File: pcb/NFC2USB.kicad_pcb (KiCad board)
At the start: 4 copper layers, 39 x 40 mm, 44 parts, among them J1 USB_C_USB2.0, SW1 BOOTSEL, SW2 MODE, U1 NFCModuleRC522, U2 AMS1117-3.3, U3 W25Q32JVUU, U4 RP2040, Y1 12MHz

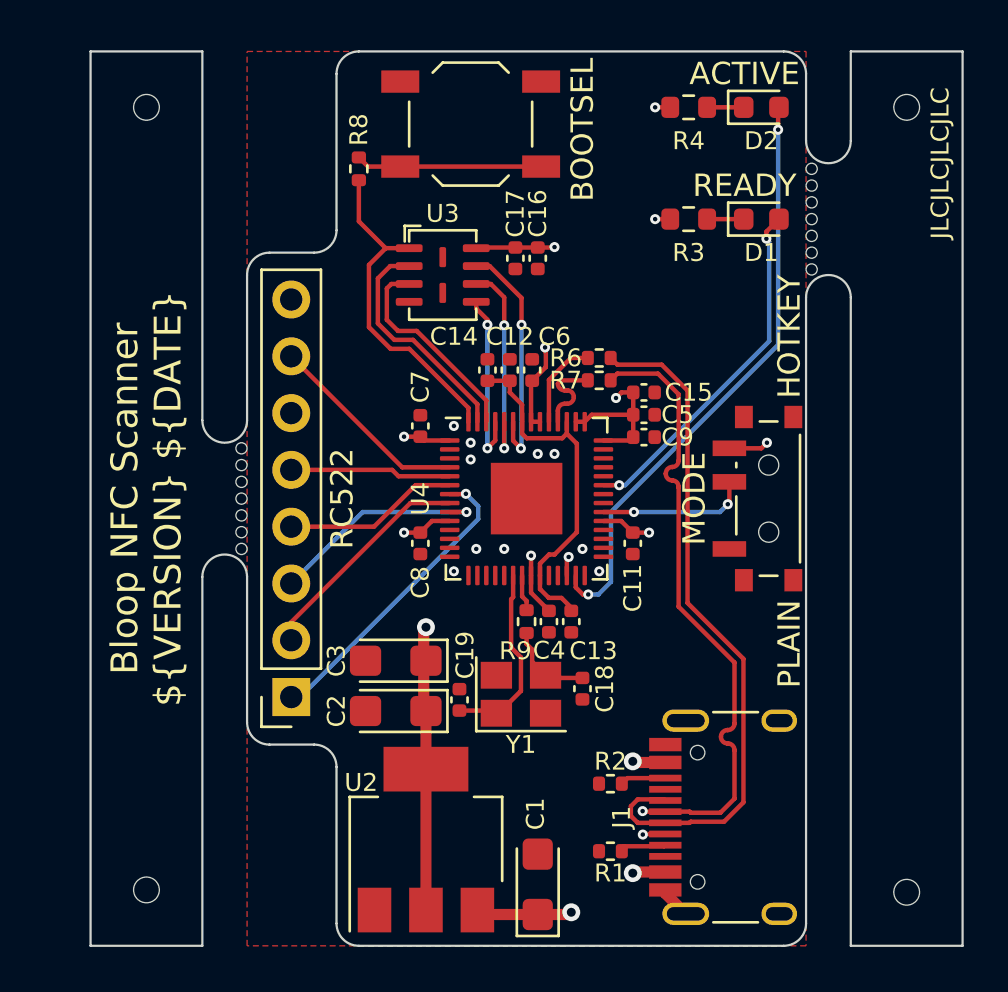
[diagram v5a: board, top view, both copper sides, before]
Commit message: fix: change mouse bites position, add silkscreen
This commit includes the switch to KiCad 7 which is why there are so many unrelated changes in the files
The mousebites were moved away from the mode switch
Silkscreen text was added for mode switch and LEDs
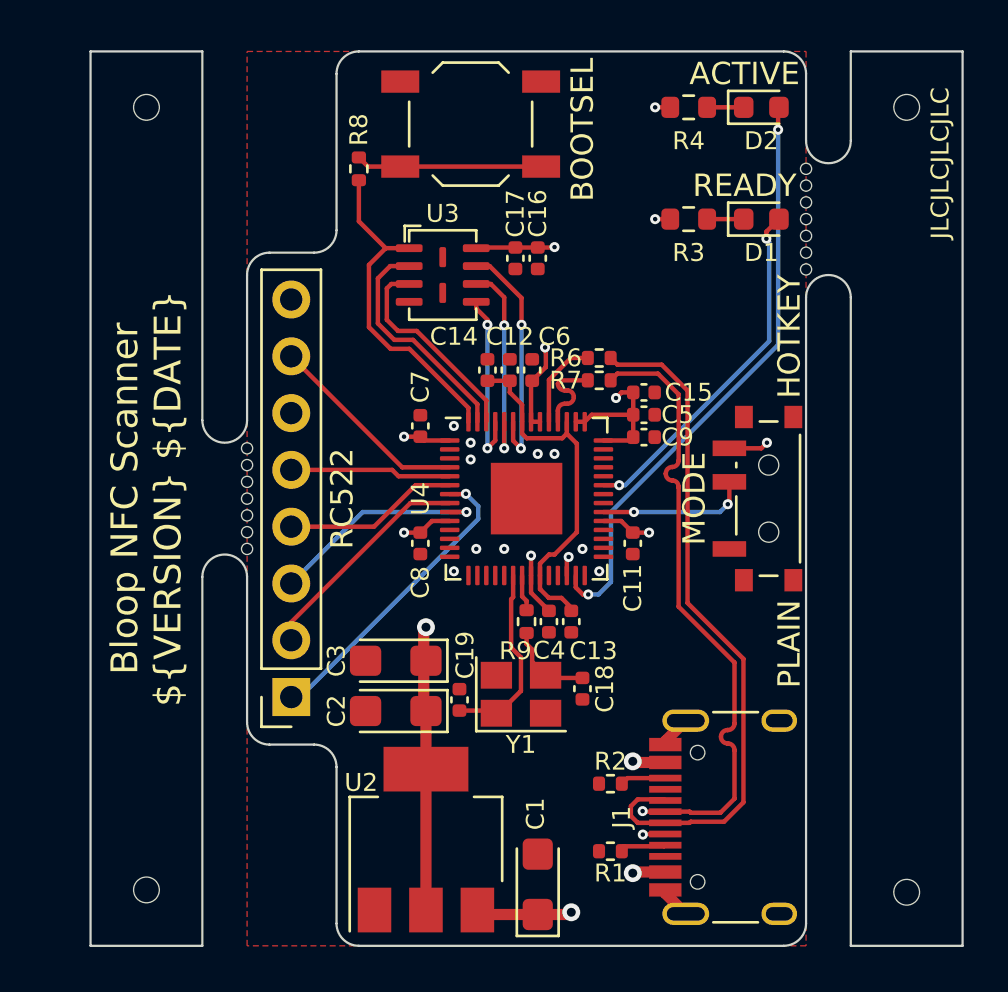
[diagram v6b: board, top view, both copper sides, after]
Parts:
- mouse-bite-2mm-slot (x2): footprint Panelization:mouse-bite-2x5mm-slot-onesided -> Panelization:mouse-bite-2x5mm-slot-onesided-v2
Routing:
- net GND: track 2.80 -> 4.25 mm

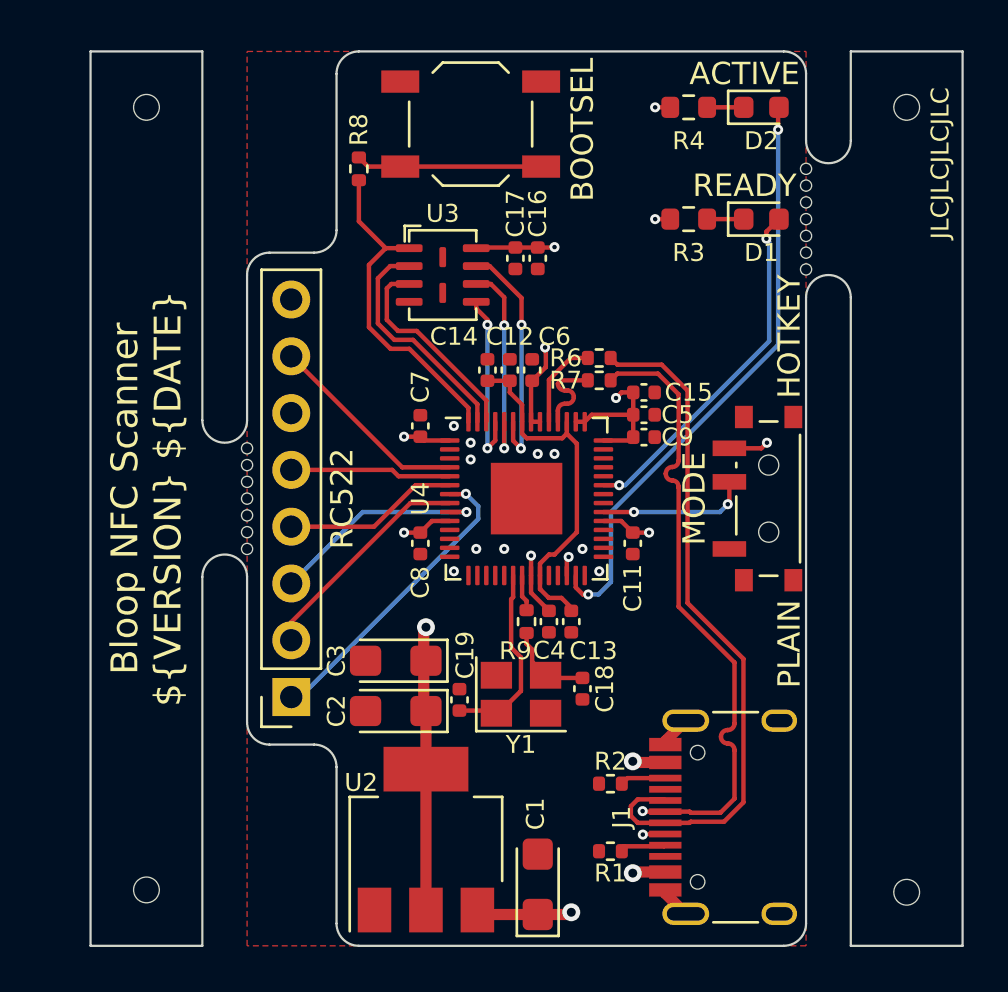
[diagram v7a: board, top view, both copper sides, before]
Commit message: fix: add part number for connector
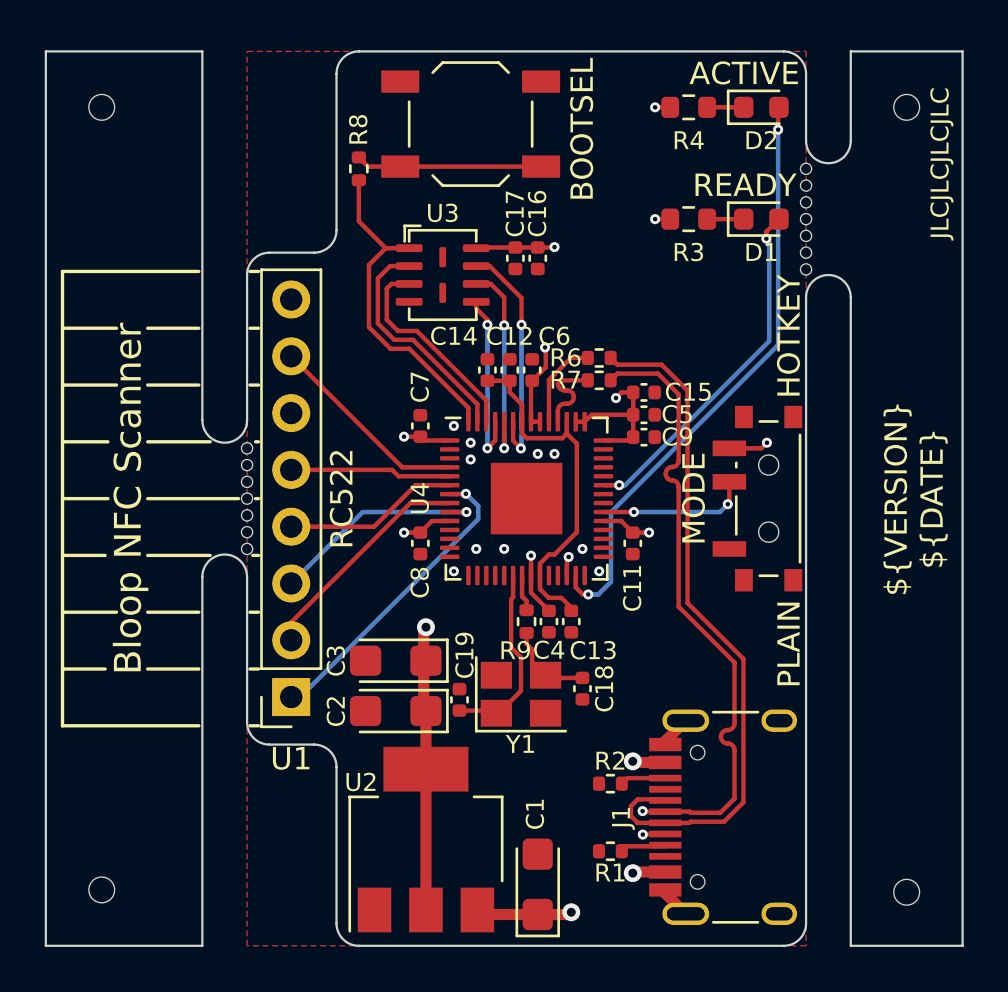
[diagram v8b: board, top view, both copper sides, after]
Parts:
- moved REF** 2.00 mm to (93.5, 87.5)
- moved REF** 2.00 mm to (93.5, 52.5)
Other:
- board size 39 x 40 mm -> 41 x 40 mm
- board text added: "${TITLE}"
- board text added: "${VERSION} ${DATE}"
